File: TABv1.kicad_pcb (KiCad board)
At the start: 2 copper layers, 0 parts

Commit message: bozza layout pcb
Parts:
- added C1: 4.7u, Capacitor_SMD:C_0603_1608Metric_Pad1.08x0.95mm_HandSolder, F.Cu at (93.5, 54.2)
- added C10: 100n, Capacitor_SMD:C_0603_1608Metric_Pad1.08x0.95mm_HandSolder, F.Cu at (81.9, 65.5)
- added C11: 100n, Capacitor_SMD:C_0603_1608Metric_Pad1.08x0.95mm_HandSolder, F.Cu at (93.0, 71.8)
- added C12: 100n, Capacitor_SMD:C_0603_1608Metric_Pad1.08x0.95mm_HandSolder, F.Cu at (81.9, 61.5)
- added C13: 100n, Capacitor_SMD:C_0603_1608Metric_Pad1.08x0.95mm_HandSolder, F.Cu at (99.6, 62.6)
- added C14: 100n, Capacitor_SMD:C_0603_1608Metric_Pad1.08x0.95mm_HandSolder, F.Cu at (95.0, 71.8)
- added C15: 100n, Capacitor_SMD:C_0603_1608Metric_Pad1.08x0.95mm_HandSolder, F.Cu at (81.9, 63.5)
- added C16: 15p, Capacitor_SMD:C_0603_1608Metric_Pad1.08x0.95mm_HandSolder, F.Cu at (76.7, 67.9)
- added C17: 15p, Capacitor_SMD:C_0603_1608Metric_Pad1.08x0.95mm_HandSolder, F.Cu at (76.6, 74.9)
- added C2: 4.7u, Capacitor_SMD:C_0603_1608Metric_Pad1.08x0.95mm_HandSolder, F.Cu at (93.5, 56.0)
- added C20: 100 nF, Capacitor_SMD:C_0603_1608Metric_Pad1.08x0.95mm_HandSolder, F.Cu at (144.1, 47.3)
- added C21: 10 uF, Capacitor_SMD:C_0603_1608Metric_Pad1.08x0.95mm_HandSolder, F.Cu at (144.1, 49.3)
- added C22: 3x22 uF, Capacitor_SMD:C_0603_1608Metric_Pad1.08x0.95mm_HandSolder, F.Cu at (144.1, 51.3)
- added C25: 100nF, Capacitor_SMD:C_0603_1608Metric_Pad1.08x0.95mm_HandSolder, F.Cu at (84.1, 74.5)
- added C26: 100nF, Capacitor_SMD:C_0603_1608Metric_Pad1.08x0.95mm_HandSolder, F.Cu at (86.6, 72.0)
- added C27: 100nF, Capacitor_SMD:C_0603_1608Metric_Pad1.08x0.95mm_HandSolder, F.Cu at (103.7, 53.2)
- added C28: 100nF, Capacitor_SMD:C_0603_1608Metric_Pad1.08x0.95mm_HandSolder, F.Cu at (107.0, 50.1)
- added C29: 100nF, Capacitor_SMD:C_0603_1608Metric_Pad1.08x0.95mm_HandSolder, F.Cu at (81.6, 53.9)
- added C3: 4.7u, Capacitor_SMD:C_0603_1608Metric_Pad1.08x0.95mm_HandSolder, F.Cu at (98.0, 55.9)
- added C30: 100nF, Capacitor_SMD:C_0603_1608Metric_Pad1.08x0.95mm_HandSolder, F.Cu at (79.0, 56.5)
- added C31: 100nF, Capacitor_SMD:C_0603_1608Metric_Pad1.08x0.95mm_HandSolder, F.Cu at (133.0, 36.1)
- added C32: 10uF, Capacitor_SMD:C_0603_1608Metric_Pad1.08x0.95mm_HandSolder, F.Cu at (112.5, 36.1)
- added C33: 220n, Capacitor_SMD:C_0603_1608Metric_Pad1.08x0.95mm_HandSolder, F.Cu at (70.2, 65.9)
- added C34: 100n, Capacitor_SMD:C_0603_1608Metric_Pad1.08x0.95mm_HandSolder, F.Cu at (69.9, 60.9)
- added C35: 10u, Capacitor_SMD:C_0603_1608Metric_Pad1.08x0.95mm_HandSolder, F.Cu at (74.6, 62.9)
- added C36: 100n, Capacitor_SMD:C_0603_1608Metric_Pad1.08x0.95mm_HandSolder, F.Cu at (72.6, 62.9)
- added C4: 100n, Capacitor_SMD:C_0603_1608Metric_Pad1.08x0.95mm_HandSolder, F.Cu at (106.4, 39.5)
- added C5: 100n, Capacitor_SMD:C_0603_1608Metric_Pad1.08x0.95mm_HandSolder, F.Cu at (85.1, 54.9)
- added C6: 100n, Capacitor_SMD:C_0603_1608Metric_Pad1.08x0.95mm_HandSolder, F.Cu at (99.6, 59.4)
- added C7: 100n, Capacitor_SMD:C_0603_1608Metric_Pad1.08x0.95mm_HandSolder, F.Cu at (99.6, 64.4)
- added C8: 100n, Capacitor_SMD:C_0603_1608Metric_Pad1.08x0.95mm_HandSolder, F.Cu at (99.6, 66.6)
- added C9: 100n, Capacitor_SMD:C_0603_1608Metric_Pad1.08x0.95mm_HandSolder, F.Cu at (91.0, 71.8)
- added D1: D_Schottky_Small, SDM2U30CSP:SDM2U30CSP, F.Cu at (152.2, 40.8)
- added D2: D_Schottky_Small, SDM2U30CSP:SDM2U30CSP, F.Cu at (152.1, 42.3)
- added H1: MountingHole, MountingHole:MountingHole_2.2mm_M2, F.Cu at (68.6, 75.9)
- added H2: MountingHole, MountingHole:MountingHole_2.2mm_M2, F.Cu at (68.8, 39.4)
- added H3: MountingHole, MountingHole:MountingHole_2.2mm_M2, F.Cu at (138.6, 78.9)
- added H4: MountingHole, MountingHole:MountingHole_2.2mm_M2, F.Cu at (142.1, 37.9)
- added IC1: TPS630702RNMR, TPS63070:TPS630701RNMR, F.Cu at (149.1, 47.4)
- added J1: USB_C_Receptacle_USB2.0_16P, Connector_USB:USB_C_Receptacle_GCT_USB4105-xx-A_16P_TopMnt_Horizontal, F.Cu at (81.7, 36.8)
- added J10: Conn_UART_HOST, Connector_PinHeader_2.54mm:PinHeader_1x02_P2.54mm_Vertical, F.Cu at (68.8, 46.4)
- added J11: Conn_UART_1, Connector_PinHeader_2.54mm:PinHeader_1x02_P2.54mm_Vertical, F.Cu at (68.8, 50.4)
- added J12: Conn_UART_0, Connector_PinHeader_2.54mm:PinHeader_1x02_P2.54mm_Vertical, F.Cu at (68.8, 54.4)
- added J13: Conn_ADC, Connector_PinHeader_2.54mm:PinHeader_1x04_P2.54mm_Vertical, F.Cu at (104.3, 81.0)
- added J14: Conn_BATT, Connector_PinHeader_2.54mm:PinHeader_1x02_P2.54mm_Vertical, F.Cu at (142.3, 42.3)
- added J15: DB141R-2.54-8P-GN, DB141R-2-54-8:CONN16_DB141R_DIO, F.Cu at (154.6, 59.1)
- added J6: Conn_01x03_Pin, Connector_PinHeader_2.54mm:PinHeader_1x03_P2.54mm_Vertical, F.Cu at (95.4, 81.0)
- added J7: 503398-1892, 5033981892:5033981892, F.Cu at (116.2, 34.2)
- added J8: Conn_SPI1, Connector_PinHeader_2.54mm:PinHeader_1x04_P2.54mm_Vertical, F.Cu at (91.8, 81.0)
- added J9: Conn_SPI0, Connector_PinHeader_2.54mm:PinHeader_1x04_P2.54mm_Vertical, F.Cu at (80.5, 81.0)
- added L1: 3.3u directional, Inductor_SMD:L_0805_2012Metric_Pad1.15x1.40mm_HandSolder, F.Cu at (93.4, 52.2)
- added L2: 1.5 uH, Inductor_SMD:L_1206_3216Metric_Pad1.42x1.75mm_HandSolder, F.Cu at (154.1, 47.3)
- added Q1: MJD44H11T4G, easyeda2kicad:TO-252-2_L6.5-W6.1-P4.58-LS10.0-TL, F.Cu at (112.3, 64.0)
- added Q10: PJM09P30DF, easyeda2kicad:DFN-6_L2.0-W2.0-P0.65-BL-EP-1, F.Cu at (137.8, 54.5)
- added Q11: PJM09P30DF, easyeda2kicad:DFN-6_L2.0-W2.0-P0.65-BL-EP-1, F.Cu at (137.5, 66.4)
- added Q12: PJM09P30DF, easyeda2kicad:DFN-6_L2.0-W2.0-P0.65-BL-EP-1, F.Cu at (127.5, 54.3)
- added Q13: PJM09P30DF, easyeda2kicad:DFN-6_L2.0-W2.0-P0.65-BL-EP-1, F.Cu at (127.6, 66.4)
- added Q5: NMOS, Package_TO_SOT_SMD:SOT-23_Handsoldering, F.Cu at (117.3, 73.6)
- added Q6: NMOS, Package_TO_SOT_SMD:SOT-23_Handsoldering, F.Cu at (134.8, 61.0)
- added Q7: NMOS, Package_TO_SOT_SMD:SOT-23_Handsoldering, F.Cu at (134.5, 72.9)
- added Q8: NMOS, Package_TO_SOT_SMD:SOT-23_Handsoldering, F.Cu at (124.5, 60.8)
- added Q9: NMOS, Package_TO_SOT_SMD:SOT-23_Handsoldering, F.Cu at (124.6, 72.9)
- added R1: 33, Resistor_SMD:R_0603_1608Metric_Pad0.98x0.95mm_HandSolder, F.Cu at (98.0, 52.3)
- added R12: 1k, Resistor_SMD:R_0603_1608Metric_Pad0.98x0.95mm_HandSolder, F.Cu at (133.8, 58.0)
- added R13: 40k, Resistor_SMD:R_0603_1608Metric_Pad0.98x0.95mm_HandSolder, F.Cu at (114.0, 70.4)
- added R14: 10k, Resistor_SMD:R_0603_1608Metric_Pad0.98x0.95mm_HandSolder, F.Cu at (137.8, 58.0)
- added R15: 1k, Resistor_SMD:R_0603_1608Metric_Pad0.98x0.95mm_HandSolder, F.Cu at (133.5, 69.9)
- added R16: 10k, Resistor_SMD:R_0603_1608Metric_Pad0.98x0.95mm_HandSolder, F.Cu at (137.5, 69.9)
- added R17: 1k, Resistor_SMD:R_0603_1608Metric_Pad0.98x0.95mm_HandSolder, F.Cu at (123.5, 57.8)
- added R18: 1k, Resistor_SMD:R_0603_1608Metric_Pad0.98x0.95mm_HandSolder, F.Cu at (118.0, 76.9)
- added R19: 10k, Resistor_SMD:R_0603_1608Metric_Pad0.98x0.95mm_HandSolder, F.Cu at (114.0, 76.9)
- added R2: 1k, Resistor_SMD:R_0603_1608Metric_Pad0.98x0.95mm_HandSolder, F.Cu at (95.5, 35.9)
- added R20: 10k, Resistor_SMD:R_0603_1608Metric_Pad0.98x0.95mm_HandSolder, F.Cu at (149.6, 42.8)
- added R21: 470k, Resistor_SMD:R_0603_1608Metric_Pad0.98x0.95mm_HandSolder, F.Cu at (152.0, 51.3)
- added R22: 150k, Resistor_SMD:R_0603_1608Metric_Pad0.98x0.95mm_HandSolder, F.Cu at (148.1, 51.3)
- added R23: 100k, Resistor_SMD:R_0603_1608Metric_Pad0.98x0.95mm_HandSolder, F.Cu at (144.1, 45.3)
- added R27: 1k, Resistor_SMD:R_0603_1608Metric_Pad0.98x0.95mm_HandSolder, F.Cu at (133.8, 64.0)
- added R28: 10k, Resistor_SMD:R_0603_1608Metric_Pad0.98x0.95mm_HandSolder, F.Cu at (138.8, 62.0)
- added R29: 10k, Resistor_SMD:R_0603_1608Metric_Pad0.98x0.95mm_HandSolder, F.Cu at (113.0, 73.6)
- added R3: 10k, Resistor_SMD:R_0603_1608Metric_Pad0.98x0.95mm_HandSolder, F.Cu at (99.0, 36.8)
- added R30: 1k, Resistor_SMD:R_0603_1608Metric_Pad0.98x0.95mm_HandSolder, F.Cu at (133.5, 75.9)
- added R31: 10k, Resistor_SMD:R_0603_1608Metric_Pad0.98x0.95mm_HandSolder, F.Cu at (138.5, 73.9)
- added R32: 1k, Resistor_SMD:R_0603_1608Metric_Pad0.98x0.95mm_HandSolder, F.Cu at (123.5, 63.8)
- added R33: 10k, Resistor_SMD:R_0603_1608Metric_Pad0.98x0.95mm_HandSolder, F.Cu at (128.5, 61.8)
- added R34: 10k, Resistor_SMD:R_0603_1608Metric_Pad0.98x0.95mm_HandSolder, F.Cu at (127.5, 57.8)
- added R35: 1k, Resistor_SMD:R_0603_1608Metric_Pad0.98x0.95mm_HandSolder, F.Cu at (123.6, 75.9)
- added R36: 10k, Resistor_SMD:R_0603_1608Metric_Pad0.98x0.95mm_HandSolder, F.Cu at (128.6, 73.9)
- added R37: 1k, Resistor_SMD:R_0603_1608Metric_Pad0.98x0.95mm_HandSolder, F.Cu at (123.6, 69.9)
- added R38: 10k, Resistor_SMD:R_0603_1608Metric_Pad0.98x0.95mm_HandSolder, F.Cu at (127.6, 69.9)
- added R4: 1k, Resistor_SMD:R_0603_1608Metric_Pad0.98x0.95mm_HandSolder, F.Cu at (72.6, 71.4)
- added R40: 10k, Resistor_SMD:R_0603_1608Metric_Pad0.98x0.95mm_HandSolder, F.Cu at (121.8, 50.6)
- added R5: 27, Resistor_SMD:R_0603_1608Metric_Pad0.98x0.95mm_HandSolder, F.Cu at (87.6, 51.4)
- added R6: 27, Resistor_SMD:R_0603_1608Metric_Pad0.98x0.95mm_HandSolder, F.Cu at (89.4, 51.4)
- added R7: 1k, Resistor_SMD:R_0603_1608Metric_Pad0.98x0.95mm_HandSolder, F.Cu at (105.8, 76.1)
- added R8: 200k, Resistor_SMD:R_0603_1608Metric_Pad0.98x0.95mm_HandSolder, F.Cu at (109.3, 54.5)
- added R9: 100, Resistor_SMD:R_0603_1608Metric_Pad0.98x0.95mm_HandSolder, F.Cu at (109.3, 56.5)
- added RN6: 24k, Resistor_SMD:R_Array_Convex_4x0603, F.Cu at (112.5, 40.4)
- added RN7: 47, Resistor_SMD:R_Array_Convex_4x0603, F.Cu at (112.5, 44.6)
- added RN8: 24k, Resistor_SMD:R_Array_Convex_4x0603, F.Cu at (133.0, 40.4)
- added RN9: 47, Resistor_SMD:R_Array_Convex_4x0603, F.Cu at (133.0, 44.6)
- added SW1: BOOTSEL, TSB008:TSB008, F.Cu at (90.6, 41.9)
- added SW2: RESET, TSB008:TSB008, F.Cu at (102.8, 73.6)
- added U1: RP2350B-QFN80, Package_DFN_QFN:QFN-80-1EP_10x10mm_P0.4mm_EP3.4x3.4mm, F.Cu at (90.4, 62.8)
- added U2: W25Q128JVS, Package_SO:SOIC-8_5.3x5.3mm_P1.27mm, F.Cu at (99.1, 41.4)
- added U3: BMP390, bmp390:10LGA_2X2X0p75_BOS-M, F.Cu at (86.9, 74.8)
- added U4: LSM6DSO32TR, LSM6DSO32TR:LGA-14L_2P5X3X0P83_STM-M, F.Cu at (103.8, 49.9)
- added U6: LT3092xST, Package_TO_SOT_SMD:SOT-223-3_TabPin2, F.Cu at (116.4, 56.7)
- added U7: LSM6DSO32TR, LSM6DSO32TR:LGA-14L_2P5X3X0P83_STM-M, F.Cu at (78.1, 53.0)
- added U8: LIS2MDL, Package_LGA:LGA-12_2x2mm_P0.5mm, F.Cu at (70.1, 63.4)
- added Y1: 12MHz, ABM8-272-T3:ABM8272T3, F.Cu at (76.7, 71.4)
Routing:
- net /LX: track 0.00 -> 5.20 mm
- net /AVDD: track 0.00 -> 1.83 mm
- added copper zone on F.Cu, net +1V1
- added copper zone on B.Cu, net +3V3
- added copper zone on F.Cu, net -BATT
- added copper zone on F.Cu, net /LX
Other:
- board outline added: 95 x 49.5 mm
- copper layers 2 -> 4

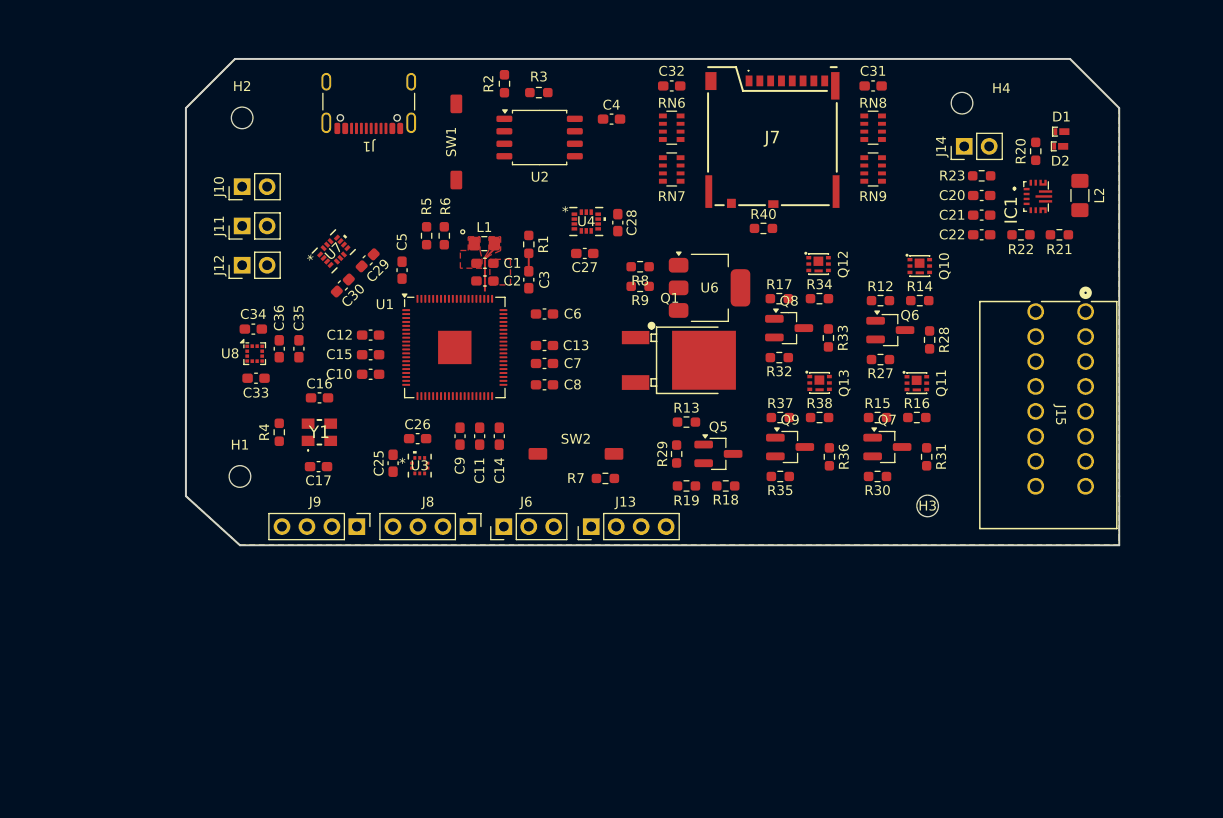
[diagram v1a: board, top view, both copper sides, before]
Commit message: ridimensionamento scheda
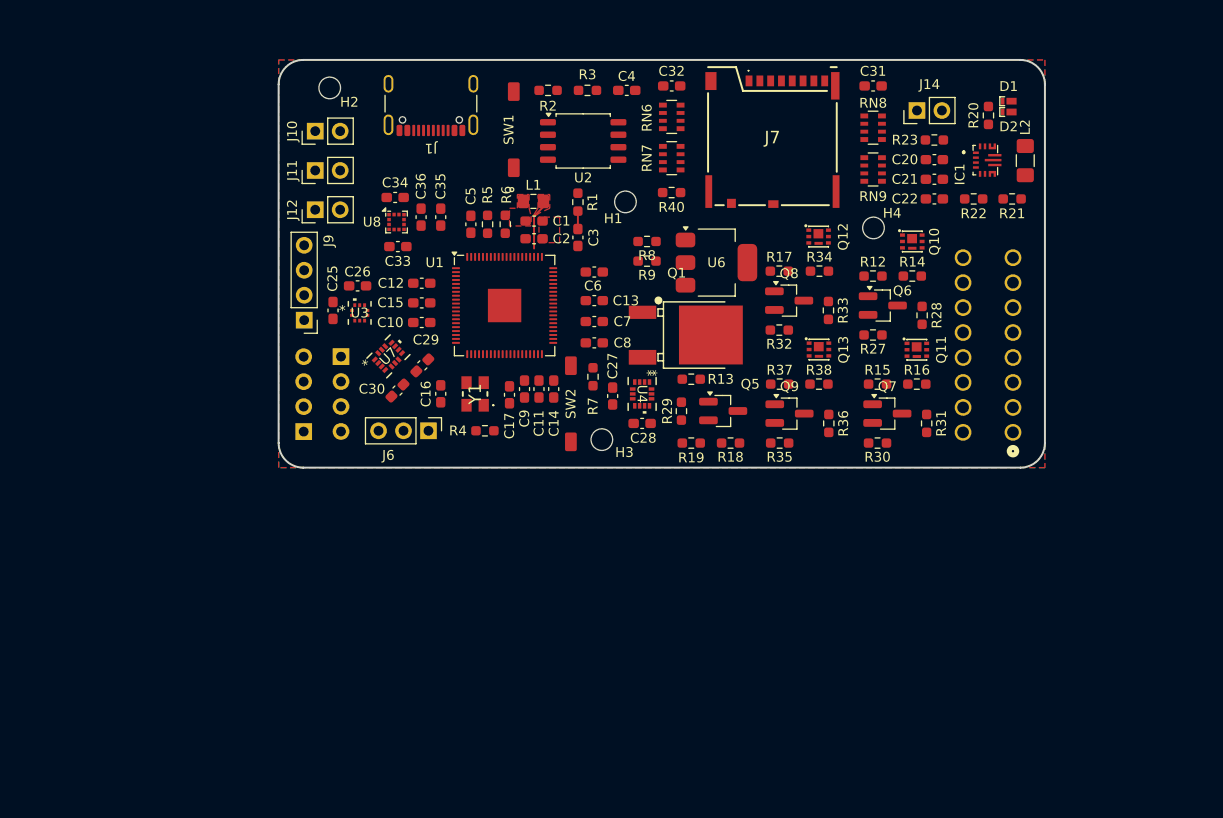
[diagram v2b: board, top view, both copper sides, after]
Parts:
- J13, J15, J8: moved to B.Cu
- J6: value Conn_01x03_Pin -> SWD
- moved H1 48.2 mm to (107.8, 48.0)
- moved H3 33.8 mm to (105.4, 72.2)
- moved J13 30.8 mm to (78.8, 63.7), turned to 180 degrees
- moved J9 21.7 mm to (75.1, 60.0), turned to 180 degrees
- moved R4 20.9 mm to (93.5, 71.2), turned to 0 degrees
- moved C17 20.8 mm to (96.0, 67.6), turned to -90 degrees
- moved C28 20.6 mm to (109.5, 70.5), turned to 0 degrees
- moved C33 19.7 mm to (84.6, 52.5)
- moved C34 19.7 mm to (84.4, 47.5)
- moved C35 19.7 mm to (89.0, 49.5)
- moved C36 19.7 mm to (87.0, 49.5)
- moved U8 19.7 mm to (84.5, 50.0)
- moved J8 19.3 mm to (75.0, 71.3), turned to 0 degrees
- moved U4 18.4 mm to (109.5, 67.5), turned to -90 degrees
- moved C25 16.7 mm to (78.0, 59.0)
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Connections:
- C21 pad 2: +3V3 -> +3.3V
- C22 pad 1: +3V3 -> +3.3V
- C34 pad 1: +3V3 -> +3.3V
- C35 pad 1: +3V3 -> +3.3V
- C36 pad 2: +3V3 -> +3.3V
- IC1 pad 7: +3V3 -> +3.3V
- IC1 pad 8: +3V3 -> +3.3V
- R21 pad 2: +3V3 -> +3.3V
- R23 pad 1: +3V3 -> +3.3V
- U8 pad 10: +3V3 -> +3.3V
- U8 pad 9: +3V3 -> +3.3V
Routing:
- added copper zone on B.Cu, net +3.3V
- removed copper zone on B.Cu, net +3V3
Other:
- board size 95 x 49.5 mm -> 78 x 41.5 mm

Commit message: ridimensionamento scheda
to do:
- aggiungere led rgb smd
- gps
- can bus
- lora/altro
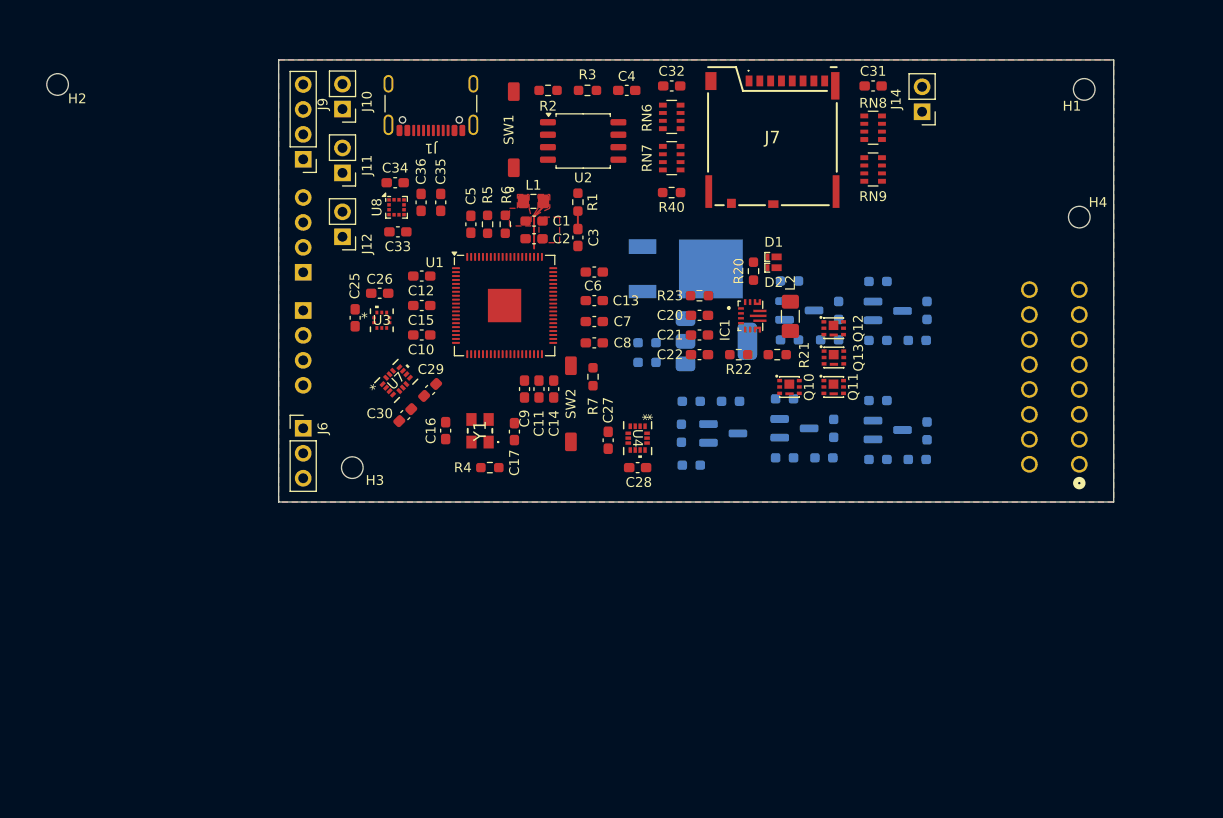
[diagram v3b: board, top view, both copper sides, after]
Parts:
- Q1, Q5, Q6, Q7, Q8, Q9, R12, R13, R14, R15, R16, R17, R18, R19, R27, R28, R29, R30, R31, R32, R33, R34, R35, R36, R37, R38, R8, R9, U6: moved to B.Cu
- moved H1 48.1 mm to (154.5, 36.5)
- moved C20 28.7 mm to (115.3, 59.5)
- moved C21 28.7 mm to (115.3, 61.5)
- moved C22 28.7 mm to (115.3, 63.5)
- moved D2 28.7 mm to (122.9, 54.6)
- moved L2 28.7 mm to (124.6, 59.6)
- moved R20 28.7 mm to (120.8, 55.0)
- moved R22 28.7 mm to (119.3, 63.5)
- moved R23 28.7 mm to (115.3, 57.5)
- moved D1 28.7 mm to (122.9, 53.5)
- moved IC1 28.7 mm to (120.0, 59.5)
- moved R21 28.7 mm to (123.3, 63.5)
- moved H2 27.7 mm to (50.0, 36.0)
- moved H3 25.6 mm to (80.0, 75.0)
- moved H4 21.0 mm to (154.0, 49.5)
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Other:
- board size 78 x 41.5 mm -> 85 x 45 mm

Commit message: inserimento servo
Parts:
- added J2: Conn_02x03_Row_Letter_Last, Connector_PinHeader_2.54mm:PinHeader_2x03_P2.54mm_Horizontal, F.Cu at (150.5, 38.5)
- added J3: Conn_02x03_Row_Letter_Last, Connector_PinHeader_2.54mm:PinHeader_2x03_P2.54mm_Horizontal, F.Cu at (150.5, 47.5)
- moved C22 33.8 mm to (146.2, 49.7), turned to 90 degrees
- moved R22 32.2 mm to (146.2, 45.7), turned to 90 degrees
- moved R21 31.6 mm to (146.2, 41.8), turned to 90 degrees
- moved C21 31.2 mm to (144.2, 49.7), turned to -90 degrees
- moved C20 28.6 mm to (142.2, 49.7), turned to 90 degrees
- moved IC1 26.6 mm to (142.2, 45.1), turned to 90 degrees
- moved L2 26.1 mm to (142.3, 40.5), turned to 180 degrees
- moved R23 26.0 mm to (140.2, 49.7), turned to 90 degrees
- moved H4 23.0 mm to (139.0, 67.0)
- moved R20 20.0 mm to (137.7, 44.2), turned to 180 degrees
- moved D2 19.9 mm to (138.1, 41.9), turned to 90 degrees
- moved D1 18.3 mm to (137.0, 41.9), turned to 90 degrees
- moved H1 12.5 mm to (165.5, 30.5)
- moved J14 6.16 mm to (143.5, 36.0), turned to -90 degrees
- moved J15 2.47 mm to (154.0, 77.1)
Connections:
- net Net-(J9-Pin_1) renamed /PWM4
- net Net-(J9-Pin_2) renamed /PWM3
- net Net-(J9-Pin_3) renamed /PWM2
- net Net-(J9-Pin_4) renamed /PWM1

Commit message: led e buzzer
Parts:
- added D5: BLUE, LED_SMD:LED_0603_1608Metric, F.Cu at (129.7, 69.8)
- added D6: GREEN, LED_SMD:LED_0603_1608Metric, F.Cu at (129.7, 72.6)
- added D7: RED, LED_SMD:LED_0603_1608Metric, F.Cu at (129.7, 75.4)
- added LS1: CMT-8503-85B-SMT-TR, CMT-8503-85B-SMT-TR:XDCR_CMT-8503-85B-SMT-TR, F.Cu at (120.4, 57.6)
- added Q2: NMOS, Package_TO_SOT_SMD:SOT-23, F.Cu at (117.9, 66.1)
- added R10: 100, Resistor_SMD:R_0603_1608Metric_Pad0.98x0.95mm_HandSolder, F.Cu at (117.0, 70.1)
- added R11: 10K, Resistor_SMD:R_0603_1608Metric_Pad0.98x0.95mm_HandSolder, F.Cu at (119.0, 70.1)
- added RN10: 220 Ohm, Resistor_SMD:R_Array_Convex_4x0603, F.Cu at (125.7, 72.9)
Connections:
- U1 pad 36: unconnected-(U1-GPIO28-Pad36) -> /L_RED
- U1 pad 37: unconnected-(U1-GPIO29-Pad37) -> /L_GREEN
- U1 pad 56: unconnected-(U1-GPIO45_ADC5-Pad56) -> /L_BLUE
- U1 pad 57: unconnected-(U1-GPIO46_ADC6-Pad57) -> /BUZZ

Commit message: L1 footprint updated
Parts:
- added D11: LED_Small, LED_SMD:LED_0603_1608Metric, F.Cu at (81.5, 88.6)
- added D12: LED_Small, LED_SMD:LED_0603_1608Metric, F.Cu at (81.5, 91.2)
- added D8: D_Schottky, SDM2U30CSP:SDM2U30CSP, F.Cu at (81.0, 93.5)
- added D9: D_Schottky, SDM2U30CSP:SDM2U30CSP, F.Cu at (81.0, 95.5)
- added SW3: RESET, TSB008:TSB008, F.Cu at (68.8, 105.8)
- added SW4: RESET, TSB008:TSB008, F.Cu at (68.8, 108.0)
- added U10: ~, rc-wle5:RC-WLE5-XXX, F.Cu at (65.0, 103.2)
- L1: footprint Inductor_SMD:L_0805_2012Metric_Pad1.15x1.40mm_HandSolder -> AOTA B201610S3R3-101-T:L_AOTA-B201610S3R3-101-T_MCH
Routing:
- net /LX: track 5.20 -> 6.05 mm

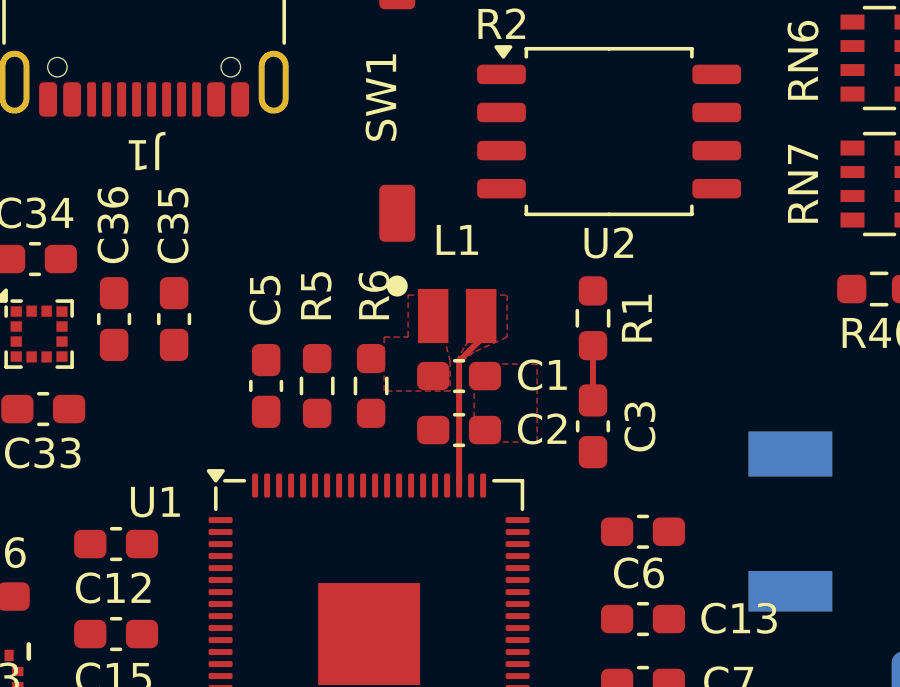
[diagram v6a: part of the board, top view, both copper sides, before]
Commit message: aggiunte tracce per regolatore spostato gnd plane al secondo layer e messo 3v3 al rpimo layer aggiunto f courtyard su bootsel switch (sw1)
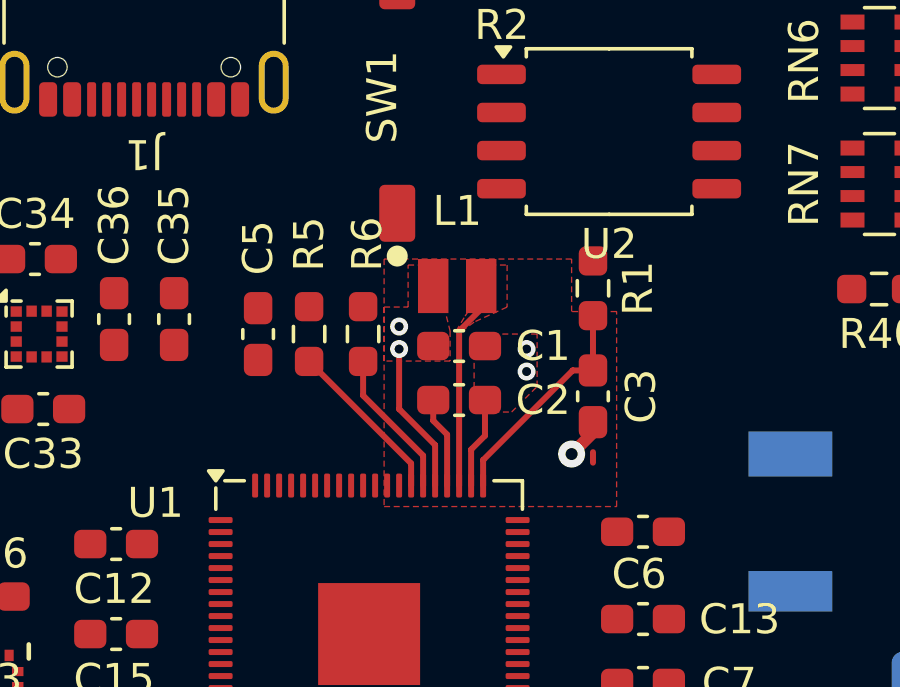
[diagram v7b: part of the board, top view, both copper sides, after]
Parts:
- moved C5 1.75 mm to (91.8, 48.5)
- moved R5 1.75 mm to (93.5, 48.5)
- moved R6 1.75 mm to (95.3, 48.5)
- moved C1 1.00 mm to (98.5, 48.9)
- moved C2 1.00 mm to (98.5, 50.7)
- moved C3 1.00 mm to (103.0, 50.6)
- moved L1 1.00 mm to (98.4, 46.9)
- moved R1 1.00 mm to (103.0, 47.0)
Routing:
- net /AVDD: track 1.82 -> 7.57 mm
- net Net-(U1-USB_DP): track 0.00 -> 5.55 mm
- net +1V1: track 0.00 -> 5.05 mm, vias 0 -> 2
- net Net-(U1-USB_DM): track 0.00 -> 4.97 mm
- net -BATT: track 0.00 -> 4.40 mm, vias 0 -> 3
- net +3.3V: track 0.00 -> 3.04 mm
- net /LX: track 6.05 -> 7.05 mm
- added copper zone on F.Cu, net +3.3V
- added copper zone on In1.Cu, net -BATT
